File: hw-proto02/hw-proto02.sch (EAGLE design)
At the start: 23 parts, among them IC1 VN5E160MSTR-E, IC2 VN5E160MSTR-E, IC3 MCP2562T, IC5 IR4427S, J1 000, J2 000, Q1 PMOS, Q2 PMOS

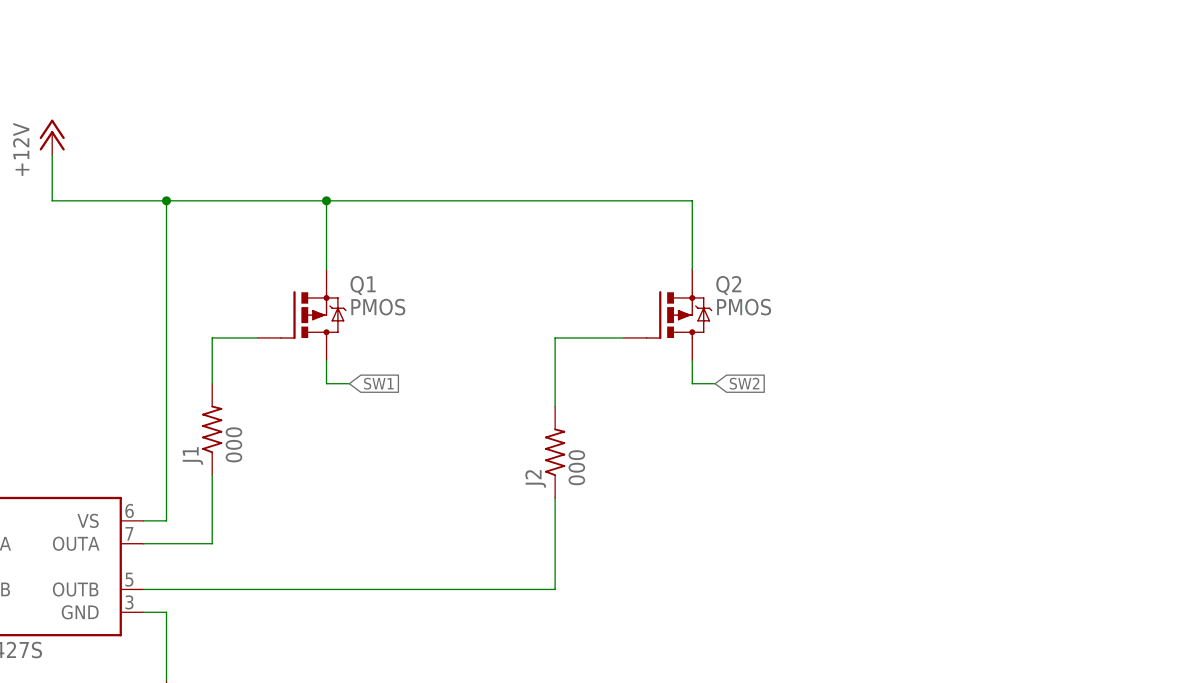
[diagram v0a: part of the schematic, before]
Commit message: changed to power-so8 fets
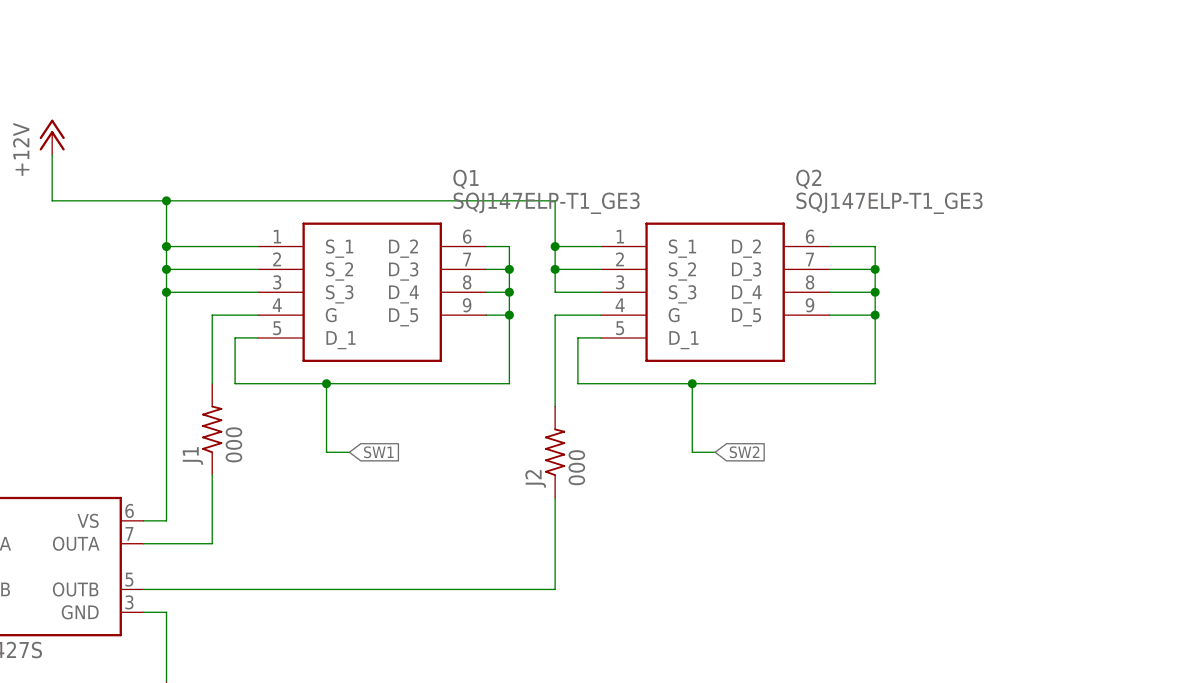
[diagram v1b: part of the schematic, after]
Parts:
- J1, J2: device rcl:R-US_0207/12 -> rcl:R-US_0204/7
- Q1, Q2: value PMOS -> SQJ147ELP-T1_GE3; device transistor-mosfet-specialpkg:IRF9530DPAK -> transistor-vishay-pchan-pso8:SQJ147ELP-T1_GE3
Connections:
- net +12V: now also Q1.S_1, Q1.S_2, Q1.S_3, Q2.S_1, Q2.S_2, Q2.S_3; no longer Q1.S, Q2.S
- net SW1: now also Q1.D_1, Q1.D_2, Q1.D_3, Q1.D_4, Q1.D_5; no longer Q1.D
- net SW2: now also Q2.D_1, Q2.D_2, Q2.D_3, Q2.D_4, Q2.D_5; no longer Q2.D

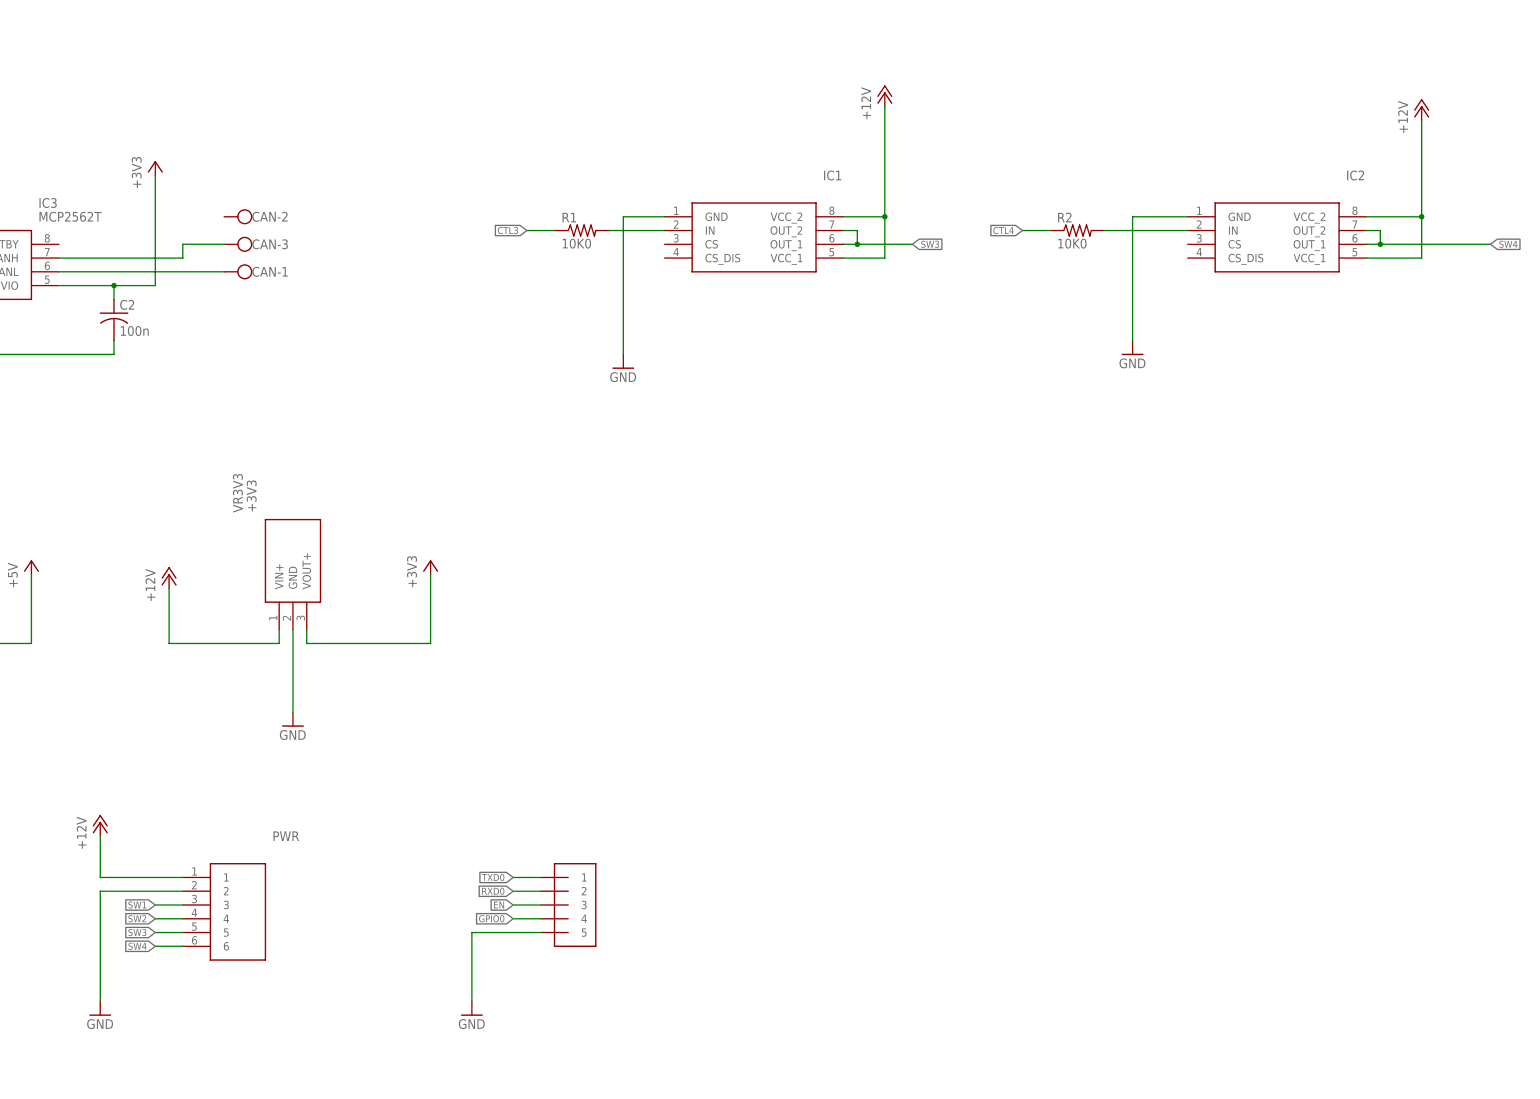
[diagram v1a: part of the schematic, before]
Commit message: made the +12v connection more chonky
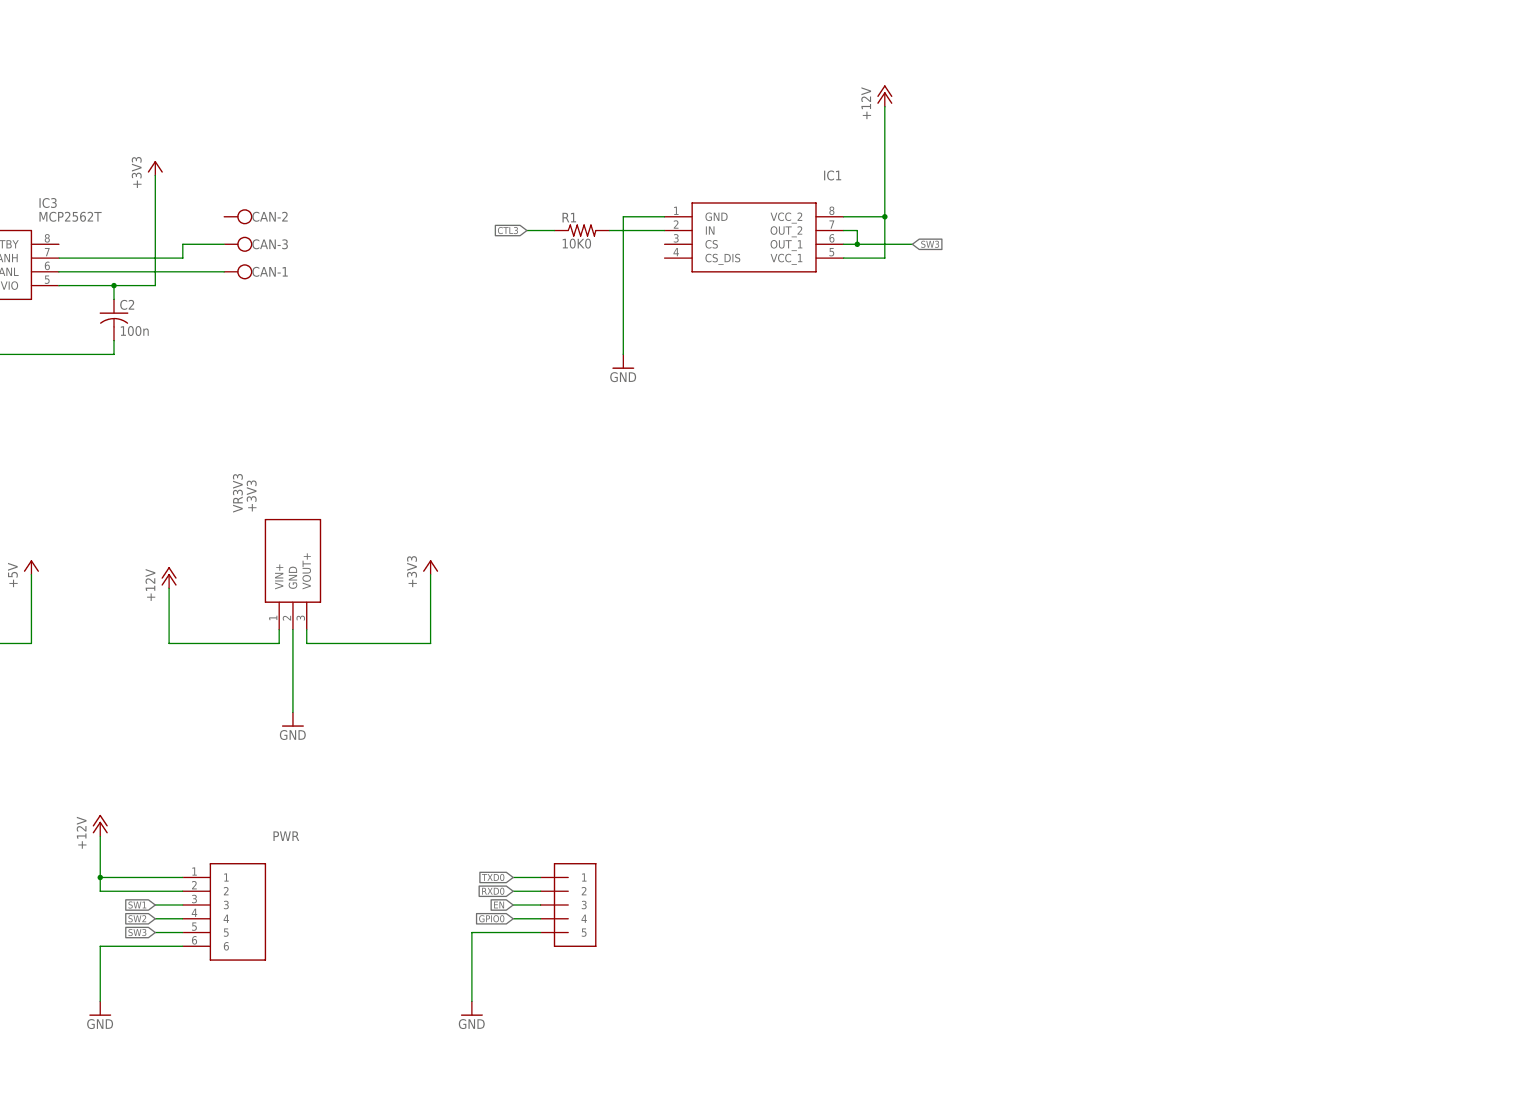
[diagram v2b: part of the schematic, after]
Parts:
- removed IC2: VN5E160MSTR-E, VN5E160MSTR-E:VN5E160MSTR-E
- removed R2: 10K0, rcl:R-US_0204/7
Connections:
- removed net N$8: IC2.IN, R2.2
- removed net SW4: IC2.OUT_1, IC2.OUT_2, PWR.6
- net +12V: now also PWR.2; no longer IC2.VCC_1, IC2.VCC_2
- net CTL4: no longer R2.1
- net GND: now also PWR.6; no longer IC2.GND, PWR.2
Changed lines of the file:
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@@
 <parts>
 <part name="IC1" library="VN5E160MSTR-E" deviceset="VN5E160MSTR-E" device="" value=""/>
-<part name="IC2" library="VN5E160MSTR-E" deviceset="VN5E160MSTR-E" device="" value=""/>
 <part name="IC3" library="MCP2562T-H_SN" deviceset="MCP2562T-H_SN" device="" value="MCP2562T"/>
 <part name="PWR" library="4DB-P108-06" deviceset="4DB-P108-06" device="" value=""/>
@@
 <part name="GND1" library="supply1" deviceset="GND" device=""/>
 <part name="GND2" library="supply1" deviceset="GND" device=""/>
-<part name="GND3" library="supply1" deviceset="GND" device=""/>
 <part name="GND5" library="supply1" deviceset="GND" device=""/>
 <part name="GND4" library="supply1" deviceset="GND" device=""/>
@@
 <part name="CAN" library="con-wago-500" deviceset="W237-103" device=""/>
 <part name="P+7" library="supply1" deviceset="+12V" device=""/>
-<part name="P+8" library="supply1" deviceset="+12V" device=""/>
 <part name="IC5" library="ir" deviceset="IR4427" device="S"/>
 <part name="GND9" library="supply1" deviceset="GND" device=""/>
@@
 <part name="J2" library="rcl" deviceset="R-US_" device="0204/7" value="000"/>
 <part name="R1" library="rcl" deviceset="R-US_" device="0204/7" value="10K0"/>
-<part name="R2" library="rcl" deviceset="R-US_" device="0204/7" value="10K0"/>
 <part name="C1" library="rcl" deviceset="C-US" device="C0603K" value="100n"/>
 <part name="C2" library="rcl" deviceset="C-US" device="C0603K" value="100n"/>
@@
 <instances>
 <instance part="IC1" gate="G$1" x="236.22" y="220.98"/>
-<instance part="IC2" gate="G$1" x="332.74" y="220.98"/>
 <instance part="IC3" gate="G$1" x="96.52" y="215.9"/>
 <instance part="PWR" gate="G$1" x="147.32" y="99.06"/>
@@
 <instance part="GND1" gate="1" x="50.8" y="152.4"/>
 <instance part="GND2" gate="1" x="228.6" y="193.04"/>
-<instance part="GND3" gate="1" x="322.58" y="195.58"/>
 <instance part="GND5" gate="1" x="-60.96" y="152.4"/>
 <instance part="GND4" gate="1" x="132.08" y="73.66"/>
@@
 <instance part="CAN" gate="-3" x="160.02" y="215.9" rot="R180"/>
 <instance part="P+7" gate="1" x="276.86" y="243.84"/>
-<instance part="P+8" gate="1" x="375.92" y="241.3"/>
 <instance part="IC5" gate="P" x="-12.7" y="45.72"/>
 <instance part="GND9" gate="1" x="2.54" y="30.48"/>
@@
 <instance part="J2" gate="G$1" x="45.72" y="58.42" rot="R90"/>
 <instance part="R1" gate="G$1" x="220.98" y="218.44"/>
-<instance part="R2" gate="G$1" x="312.42" y="218.44"/>
 <instance part="C1" gate="G$1" x="63.5" y="213.36"/>
 <instance part="C2" gate="G$1" x="134.62" y="203.2"/>
@@
 <wire x1="142.24" y1="88.9" x2="147.32" y2="88.9" width="0.1524" layer="91"/>
 <label x="142.24" y="88.9" size="1.27" layer="95" rot="R180" xref="yes"/>
-</segment>
-</net>
-<net name="SW4" class="0">
-<segment>
-<pinref part="IC2" gate="G$1" pin="OUT_1"/>
-<wire x1="365.76" y1="215.9" x2="368.3" y2="215.9" width="0.1524" layer="91"/>
-<pinref part="IC2" gate="G$1" pin="OUT_2"/>
-<wire x1="365.76" y1="218.44" x2="368.3" y2="218.44" width="0.1524" layer="91"/>
-<wire x1="368.3" y1="218.44" x2="368.3" y2="215.9" width="0.1524" layer="91"/>
-<wire x1="368.3" y1="215.9" x2="388.62" y2="215.9" width="0.1524" layer="91"/>
-<junction x="368.3" y="215.9"/>
-<label x="388.62" y="215.9" size="1.27" layer="95" xref="yes"/>
-</segment>
-<segment>
-<pinref part="PWR" gate="G$1" pin="6"/>
-<wire x1="142.24" y1="86.36" x2="147.32" y2="86.36" width="0.1524" layer="91"/>
-<label x="142.24" y="86.36" size="1.27" layer="95" rot="R180" xref="yes"/>
 </segment>
 </net>
@@
 </segment>
 <segment>
-<pinref part="PWR" gate="G$1" pin="2"/>
 <pinref part="GND4" gate="1" pin="GND"/>
-<wire x1="147.32" y1="96.52" x2="132.08" y2="96.52" width="0.1524" layer="91"/>
-<wire x1="132.08" y1="96.52" x2="132.08" y2="76.2" width="0.1524" layer="91"/>
+<wire x1="132.08" y1="86.36" x2="132.08" y2="76.2" width="0.1524" layer="91"/>
+<pinref part="PWR" gate="G$1" pin="6"/>
+<wire x1="147.32" y1="86.36" x2="132.08" y2="86.36" width="0.1524" layer="91"/>
 </segment>
 <segment>
@@
 <wire x1="236.22" y1="220.98" x2="228.6" y2="220.98" width="0.1524" layer="91"/>
 <wire x1="228.6" y1="220.98" x2="228.6" y2="195.58" width="0.1524" layer="91"/>
-</segment>
-<segment>
-<pinref part="IC2" gate="G$1" pin="GND"/>
-<wire x1="332.74" y1="220.98" x2="322.58" y2="220.98" width="0.1524" layer="91"/>
-<wire x1="322.58" y1="220.98" x2="322.58" y2="198.12" width="0.1524" layer="91"/>
-<pinref part="GND3" gate="1" pin="GND"/>
 </segment>
 <segment>
@@
 <wire x1="132.08" y1="99.06" x2="132.08" y2="106.68" width="0.1524" layer="91"/>
 <pinref part="P+2" gate="1" pin="+12V"/>
+<pinref part="PWR" gate="G$1" pin="2"/>
+<wire x1="147.32" y1="96.52" x2="132.08" y2="96.52" width="0.1524" layer="91"/>
+<wire x1="132.08" y1="96.52" x2="132.08" y2="99.06" width="0.1524" layer="91"/>
+<junction x="132.08" y="99.06"/>
 </segment>
 <segment>
@@
 <wire x1="269.24" y1="220.98" x2="276.86" y2="220.98" width="0.1524" layer="91"/>
 <junction x="276.86" y="220.98"/>
-</segment>
-<segment>
-<pinref part="IC2" gate="G$1" pin="VCC_1"/>
-<pinref part="P+8" gate="1" pin="+12V"/>
-<wire x1="365.76" y1="213.36" x2="375.92" y2="213.36" width="0.1524" layer="91"/>
-<wire x1="375.92" y1="213.36" x2="375.92" y2="220.98" width="0.1524" layer="91"/>
-<pinref part="IC2" gate="G$1" pin="VCC_2"/>
-<wire x1="375.92" y1="220.98" x2="375.92" y2="238.76" width="0.1524" layer="91"/>
-<wire x1="365.76" y1="220.98" x2="375.92" y2="220.98" width="0.1524" layer="91"/>
-<junction x="375.92" y="220.98"/>
 </segment>
 </net>
@@
 <net name="CTL4" class="0">
 <segment>
-<pinref part="R2" gate="G$1" pin="1"/>
-<wire x1="302.26" y1="218.44" x2="307.34" y2="218.44" width="0.1524" layer="91"/>
-<label x="302.26" y="218.44" size="1.27" layer="95" rot="R180" xref="yes"/>
-</segment>
-<segment>
 <pinref part="MCU" gate="G$1" pin="IO26"/>
 <wire x1="-10.16" y1="200.66" x2="-5.08" y2="200.66" width="0.1524" layer="91"/>
@@
 </segment>
 </net>
-<net name="N$8" class="0">
-<segment>
-<pinref part="R2" gate="G$1" pin="2"/>
-<pinref part="IC2" gate="G$1" pin="IN"/>
-<wire x1="317.5" y1="218.44" x2="332.74" y2="218.44" width="0.1524" layer="91"/>
-</segment>
-</net>
